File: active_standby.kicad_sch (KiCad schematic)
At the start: 13 parts, among them Q2 BSS138, U24 SN3257QDYYRQ1, U30 SN3257QDYYRQ1, U37 SN74AHC1G08QDCKRQ1

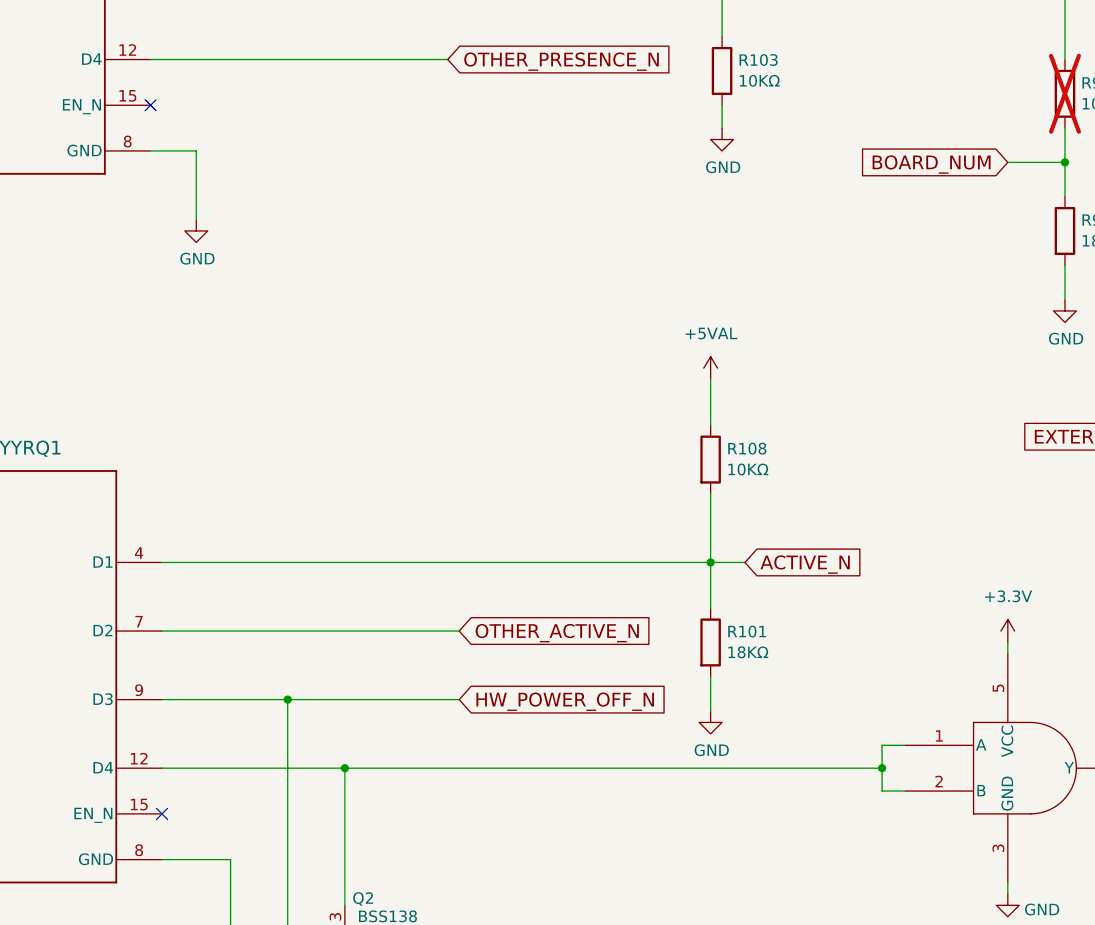
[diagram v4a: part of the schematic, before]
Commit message: Fix a reset issue with ACTIVE_N
Like the OTHER_HW_POWER_OFF_N in a previous commit, the ACTIVE_N line
was pulled low when the CPU was in reset, which could mess up fault
tolerance because ACTIVE1 controls the RF output switch.  Add a
transistor there and switch it to positive logic, ACTIVE instead.  FAULT
doesn't seem to have the issue and the rest of the lines shouldn't
matter as they are only outputs from the other board.

Signed-off-by: Corey Minyard <corey@minyard.net>
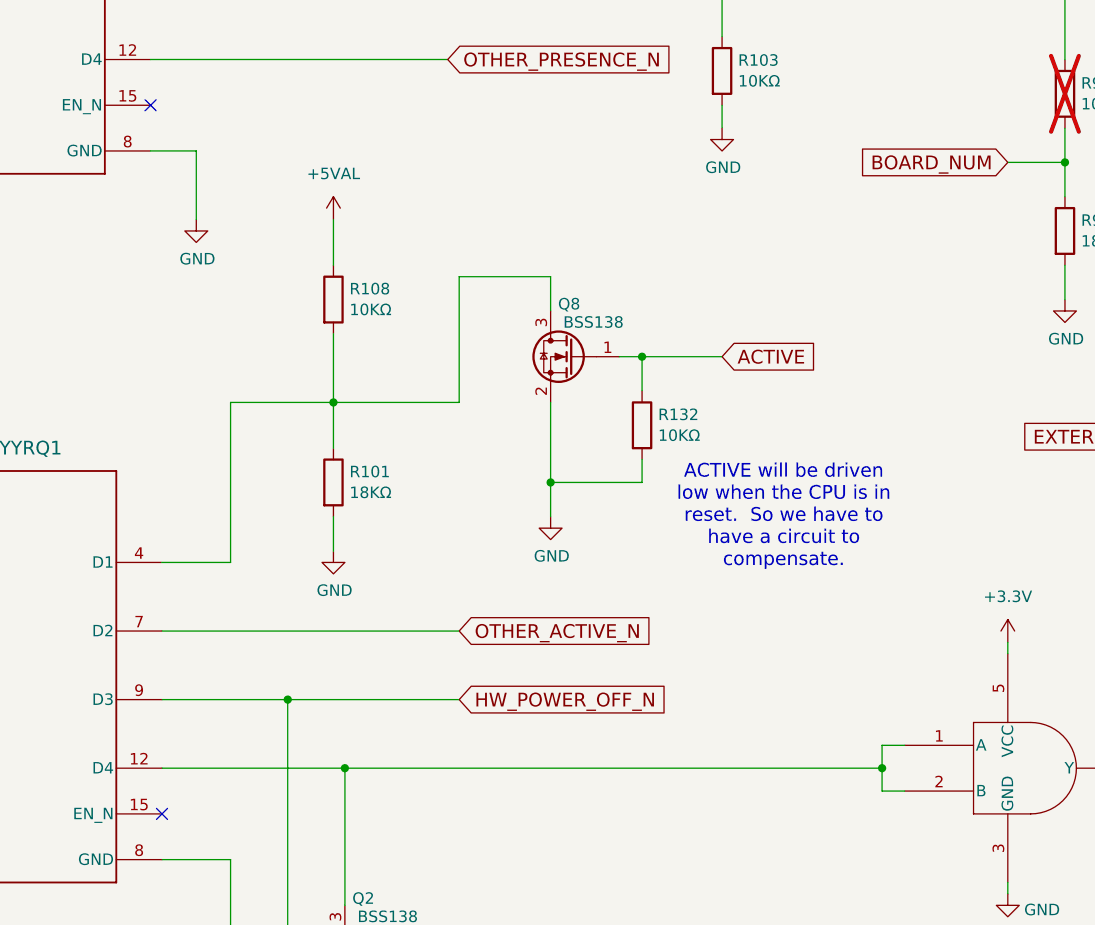
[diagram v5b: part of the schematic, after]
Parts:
- added Q8: BSS138, Package_TO_SOT_SMD:SOT-523, symbol Transistor_FET:BSS138
- added R132: 10KΩ, Resistor_SMD:R_0402_1005Metric_Pad0.72x0.64mm_HandSolder, symbol Device:R
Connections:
- net GND: now also Q8.2 (S), R132.2
- net ACTIVE_N: no longer names the net of R101.1, R108.2, U30.4 (D1)
- net ACTIVE_N: now also Q8.3 (D)
- new net ACTIVE: Q8.1 (G), R132.1
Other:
- note added: "ACTIVE will be driven low when the CPU is in reset. So we have to have a circuit to compensate."
- moved on the sheet: R101, R108

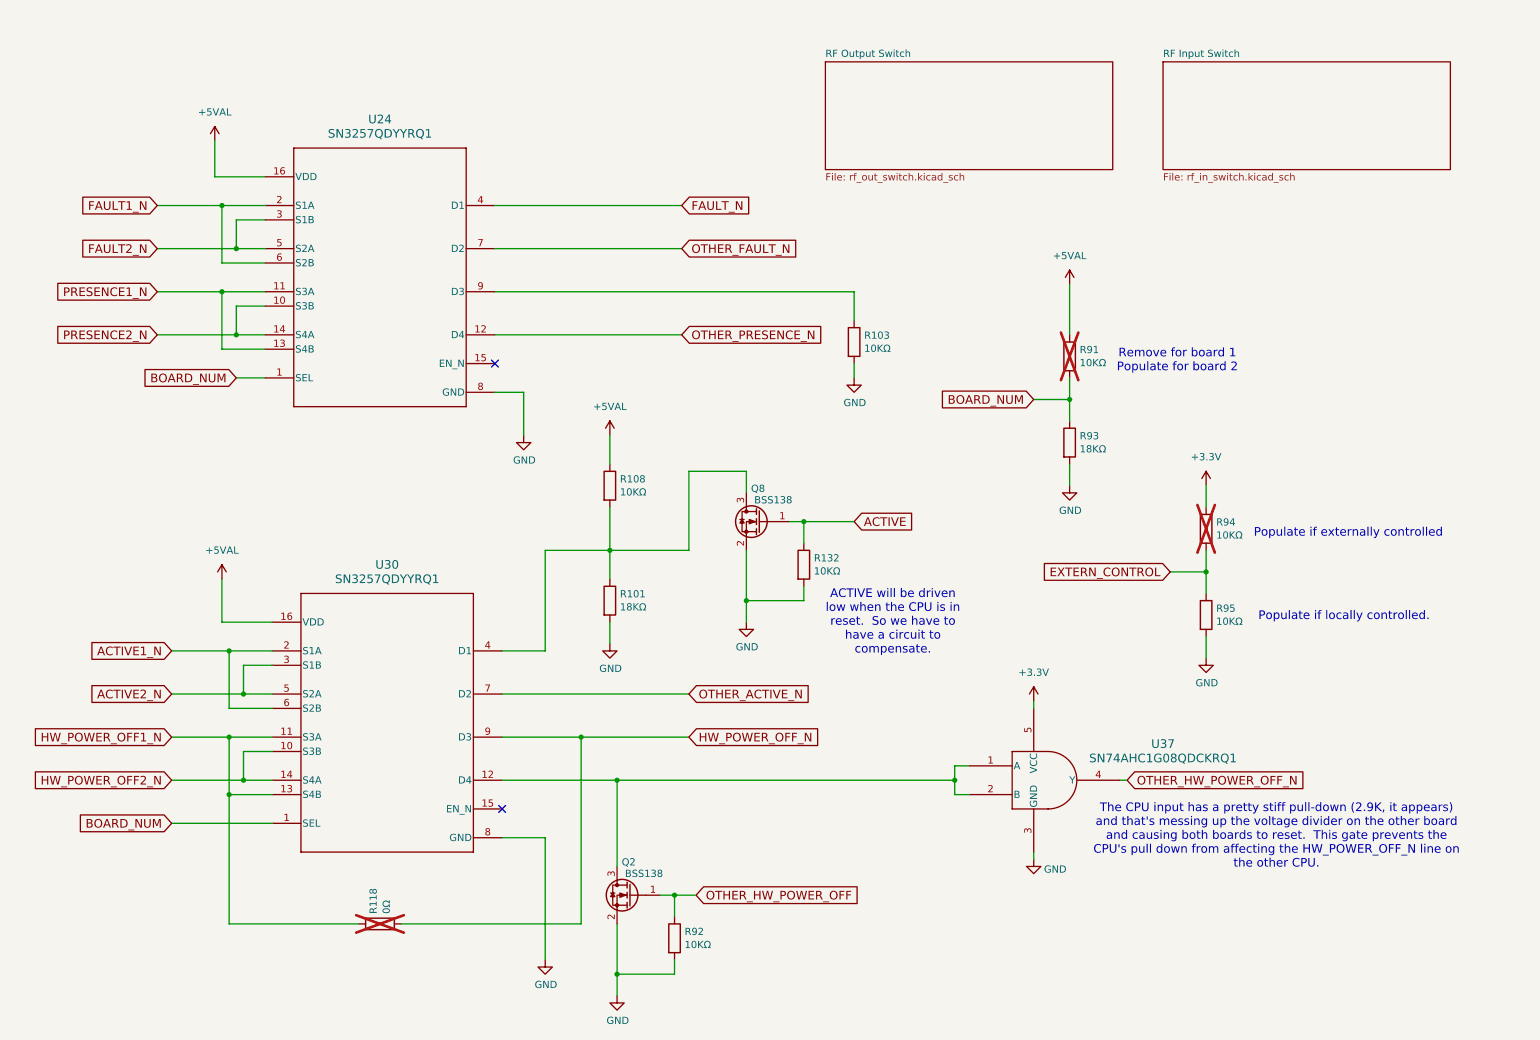
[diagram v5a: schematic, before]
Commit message: Fix latch up or pull down issues with the active/standby lines
There are either latch-up or pull-down issues when the processor is
powered off.  Make a bunch of the active/standby lines controlled
by MOSFETs to avoid this issue.

Signed-off-by: Corey Minyard <corey@minyard.net>
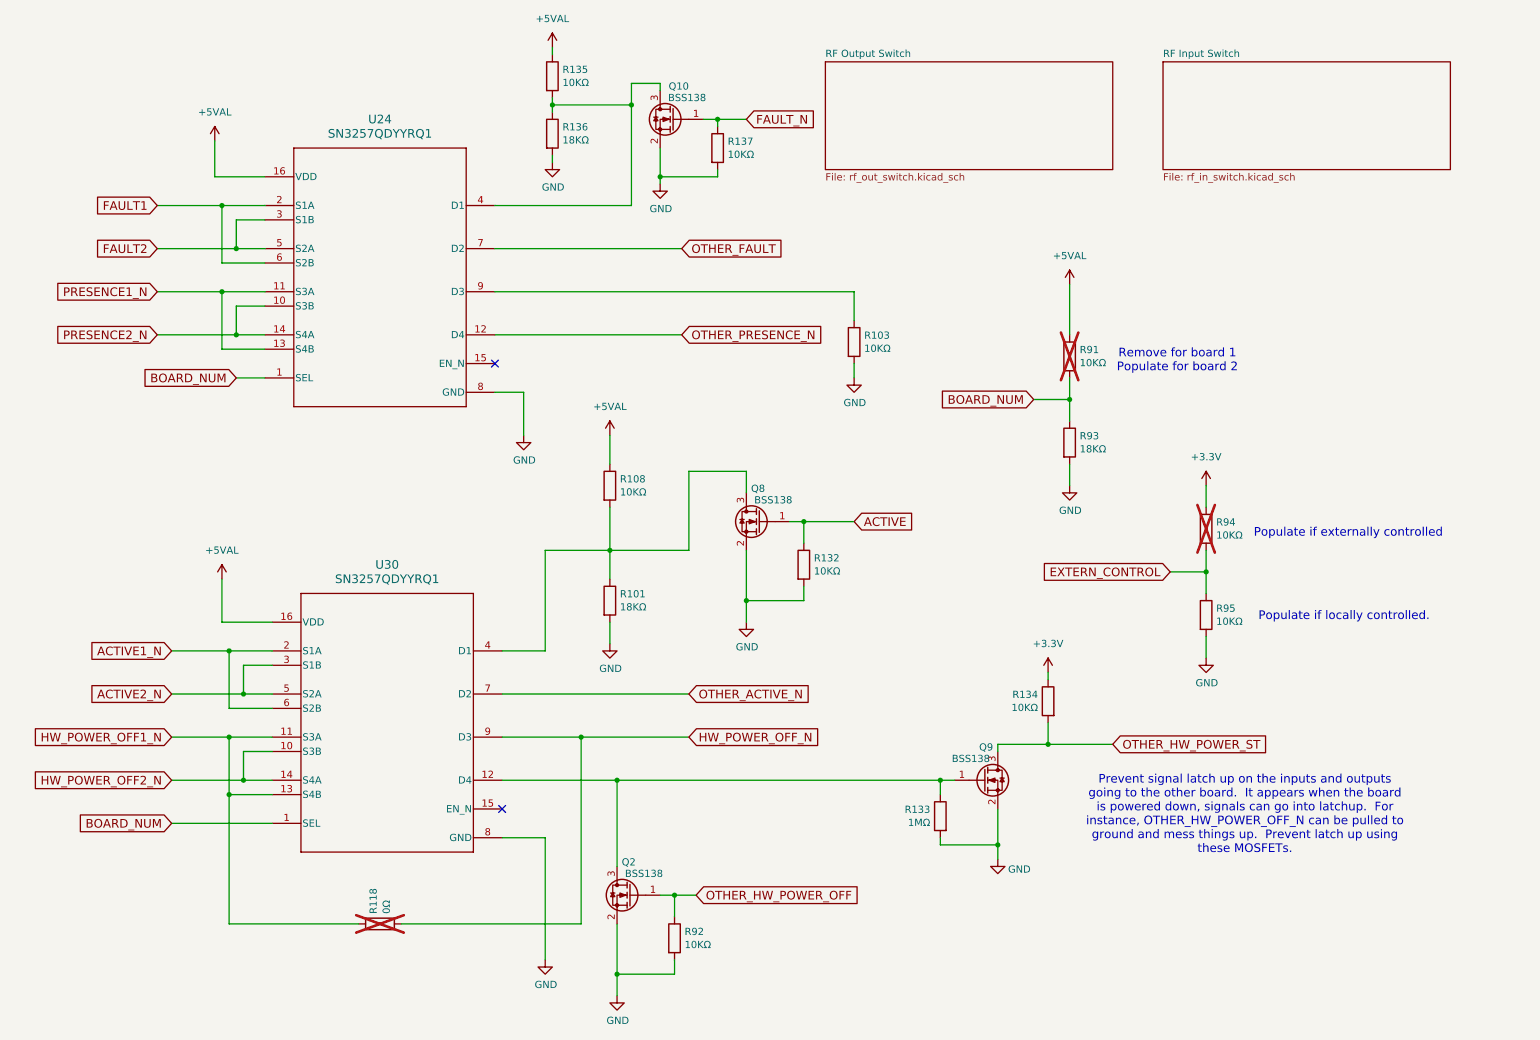
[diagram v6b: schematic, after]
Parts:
- removed U37: SN74AHC1G08QDCKRQ1, PacSatDev_ti:DCK5, symbol PACSAT_ICs:SN74AHC1G08QDCKRQ1
- added Q10, Q9: BSS138, Package_TO_SOT_SMD:SOT-523, symbol Transistor_FET:BSS138
- added R133: 1MΩ, Resistor_SMD:R_0402_1005Metric_Pad0.72x0.64mm_HandSolder, symbol Device:R
- added R134, R135, R137: 10KΩ, Resistor_SMD:R_0402_1005Metric_Pad0.72x0.64mm_HandSolder, symbol Device:R
- added R136: 18KΩ, Resistor_SMD:R_0402_1005Metric_Pad0.72x0.64mm_HandSolder, symbol Device:R
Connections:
- net +3.3V: now also R134.1
- net +5VAL: now also R135.1
- net FAULT_N: now also Q10.1 (G), R137.1; no longer U24.4 (D1)
- net GND: now also Q10.2 (S), Q9.2 (S), R133.2, R136.2, R137.2
- net at Q2.3 (D), U30.12 (D4): now also Q9.1 (G), R133.1
- net FAULT1_N renamed FAULT1
- net FAULT2_N renamed FAULT2
- net OTHER_FAULT_N renamed OTHER_FAULT
- new net: Q10.3 (D), R135.2, R136.1, U24.4 (D1)
- new net OTHER_HW_POWER_ST: Q9.3 (D), R134.2
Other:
- note added: "Prevent signal latch up on the inputs and outputs going to the other board. It appears when the board is powered down, signals can go into latchup. For instance, OTHER_HW_POWER_OFF_N can be pulled to ground and mess things up. Prevent latch up using these MOSFETs."
- note removed: "ACTIVE will be driven low when the CPU is in reset. So we have to have a circuit to compensate."
- note removed: "The CPU input has a pretty stiff pull-down (2.9K, it appears) and that's messing up the voltage divider on the other board and causing both boards to reset. This gate prevents the CPU's pull down from affecting the HW_POWER_OFF_N line on the other CPU."

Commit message: Add some more notes and docs
Signed-off-by: Corey Minyard <corey@minyard.net>
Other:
- note added: "Prevent signal latch up on the inputs and outputs going to the other board. It appears when the board is powered down, signals can go into latchup. For instance, OTHER_HW_POWER_ST can be pulled to ground and mess things up. Prevent latch up from causing problems using these MOSFETs."
- note removed: "Prevent signal latch up on the inputs and outputs going to the other board. It appears when the board is powered down, signals can go into latchup. For instance, OTHER_HW_POWER_OFF_N can be pulled to ground and mess things up. Prevent latch up using these MOSFETs."
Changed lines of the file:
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@@
 		)
 	)
-	(text "Prevent signal latch up on the inputs and outputs\ngoing to the other board.  It appears when the board\nis powered down, signals can go into latchup.  For\ninstance, OTHER_HW_POWER_OFF_N can be pulled to\nground and mess things up.  Prevent latch up using\nthese MOSFETs."
+	(text "Prevent signal latch up on the inputs and outputs\ngoing to the other board.  It appears when the board\nis powered down, signals can go into latchup.  For\ninstance, OTHER_HW_POWER_ST can be pulled to\nground and mess things up.  Prevent latch up from\ncausing problems using these MOSFETs."
 		(exclude_from_sim no)
 		(at 241.808 154.686 0)

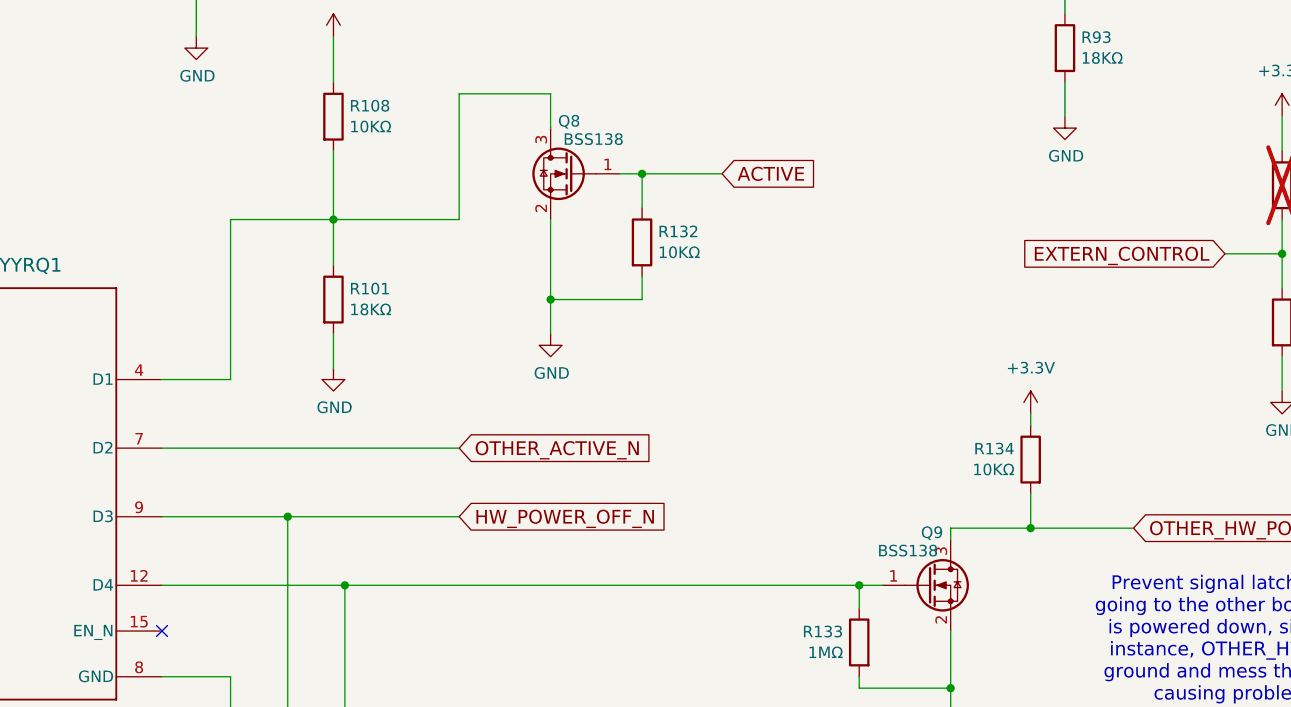
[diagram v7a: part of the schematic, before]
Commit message: Handle possible latch-up on OTHER_ACTIVE
The OTHER_ACTIVE_N line could (probably would) suffer from CMOS latch
up.  Add a MOSFET to avoid this issue, changing the polarity to the
processor in the process.

Signed-off-by: Corey Minyard <corey@minyard.net>
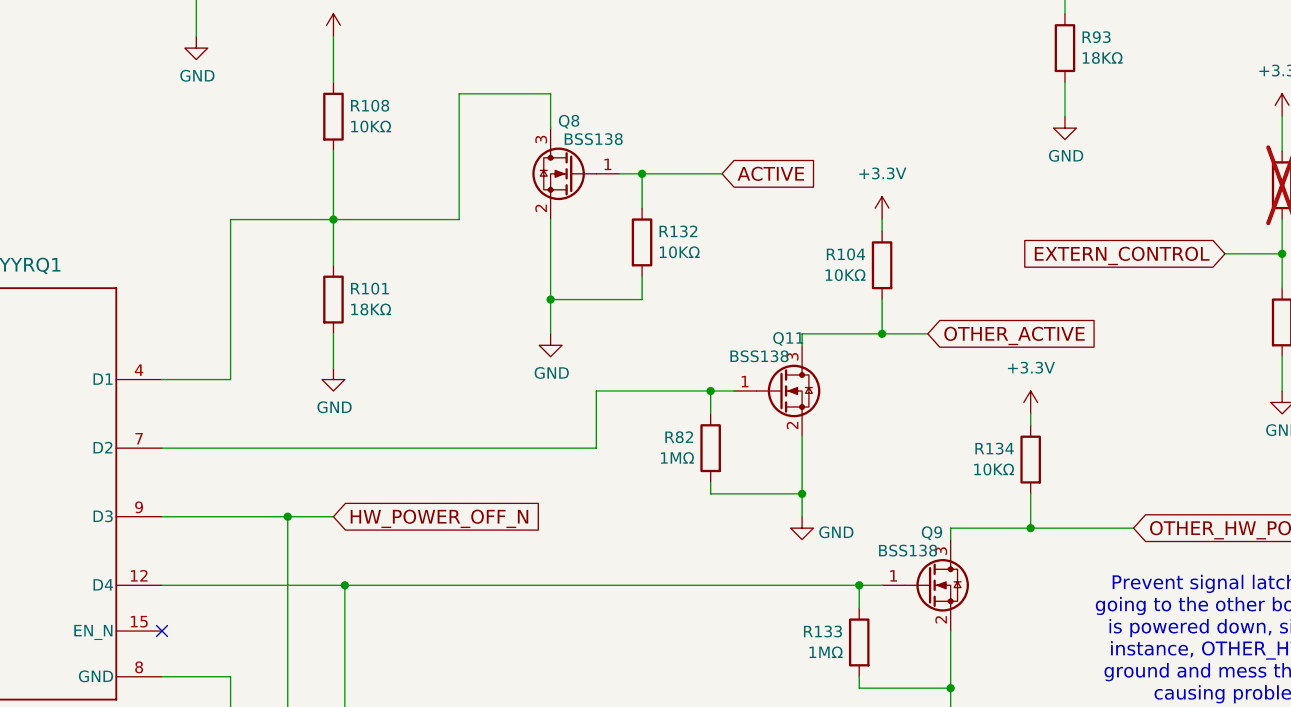
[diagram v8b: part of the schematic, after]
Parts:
- added Q11: BSS138, Package_TO_SOT_SMD:SOT-523, symbol Transistor_FET:BSS138
- added R104: 10KΩ, Resistor_SMD:R_0402_1005Metric_Pad0.72x0.64mm_HandSolder, symbol Device:R
- added R82: 1MΩ, Resistor_SMD:R_0402_1005Metric_Pad0.72x0.64mm_HandSolder, symbol Device:R
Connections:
- net +3.3V: now also R104.1
- net GND: now also Q11.2 (S), R82.2
- net OTHER_ACTIVE_N: no longer names the net of U30.7 (D2)
- net OTHER_ACTIVE_N: now also Q11.1 (G), R82.1
- new net OTHER_ACTIVE: Q11.3 (D), R104.2
